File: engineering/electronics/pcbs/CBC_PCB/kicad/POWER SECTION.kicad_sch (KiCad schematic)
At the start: 72 parts, among them J4 AMT0650009DB0000G, J5 AMT0650009DB0000G, J6 AMT0650009DB0000G, J7 AMT0650009DB0000G, Q4 SP015N03BGHTO, U10 CPC1106NTR, U11 CPC1106NTR, U12 74LVC1G17W5-7, U13 74LVC2G02HK3-7, U14 MAX810R, U15 XL7056E1, U16 1kΩ, U17 1kΩ, U18 1kΩ, U19 1kΩ, U20 1kΩ, U21 1kΩ, U22 CPC1019NTR, U31 1kΩ, U32 1kΩ

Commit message: fix: include updated CBC power section
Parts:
- removed C29, C34: 100uF, EasyEDA_Lib:CAP-TH_BD10.0-P5.00-D1.0-FD, symbol EasyEDA_Lib:LKME1252A101MF
- removed C30, C32, C33: 100nF, EasyEDA_Lib:C0603, symbol EasyEDA_Lib:CL10B104KC8NNNC
- removed D5: (no value), EasyEDA_Lib:TO-277A_L5.9-W4.4-LS6.5-TR, symbol EasyEDA_Lib:FSV10150V
- removed L3: 100uH, EasyEDA_Lib:IND-SMD_L7.1-W6.6, symbol EasyEDA_Lib:SMMS0650-101M
- removed R17: 2.7kΩ, EasyEDA_Lib:R0603, symbol EasyEDA_Lib:RT0603BRD072K7L
- removed R18: 23.7kΩ, EasyEDA_Lib:R0603, symbol EasyEDA_Lib:0603WAF2372T5E
- removed R19: 60mΩ, EasyEDA_Lib:R1206, symbol EasyEDA_Lib:JER1206F1R060
- removed U15: XL7056E1, EasyEDA_Lib:TO-263-7_L9.3-W10.0-P1.27-LB-LS15.0, symbol EasyEDA_Lib:XL7056E1
- added C36, C80, C84: 100nF, EasyEDA_Lib:C0603, symbol EasyEDA_Lib:CL10B104KC8NNNC
- added C78, C79: 2.2uF, EasyEDA_Lib:CAP-TH_BD5.0-P2.00-D0.5-FD-1, symbol EasyEDA_Lib:ERJ1KM2R2D11OT
- added C81, C82, C83: 4.7uF, EasyEDA_Lib:C0805, symbol EasyEDA_Lib:CL21A475KBQNNNE
- added D24: (no value), EasyEDA_Lib:TO-277A_L5.9-W4.4-LS6.5-TR, symbol EasyEDA_Lib:FSV10150V
- added D25: (no value), EasyEDA_Lib:SMB_L4.6-W3.6-LS5.3-BI, symbol EasyEDA_Lib:SMBJ5.0CA_C83323
- added L7: 33uH, EasyEDA_Lib:IND-SMD_L8.5-W8.0_SMS0850, symbol EasyEDA_Lib:ZEMS0850-330M
- added R49: 590K, 0603, symbol Device:R
- added R50, R52: 10kΩ, EasyEDA_Lib:R0603, symbol EasyEDA_Lib:RT0603BRD0710KL
- added R51: 140kΩ, EasyEDA_Lib:R0603, symbol EasyEDA_Lib:PTFR0603B140KP9
- added U33: MP9486GN-Z, CBC_PCB:SOIC-8EP_MP9486_MNP, symbol MP9486GN-Z:MP9486GN-Z
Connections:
- net 12V_GATE_V: now also C36.2, C81.2, C82.2, C83.2, L7.2, R49.2
- net H_PWR-IN: now also R51.2
- net H_PWR-IN-: now also C78.2, C79.2, C81.1, C82.1, C83.1, C84.1, D24.1 (A), D24.2 (A), D25.1 (K), R50.1, R52.1, U33.8 (GND)
- net at R48.1: now also C78.1, C79.1, U33.3 (VIN)
- new net: C84.2, D25.2 (A), R51.1, R52.2, U33.6 (DIM), U33.7 (EN)
- new net: C80.1, D24.3 (K), L7.1, U33.5 (SW)
- new net: C36.1, R49.1, R50.2, U33.1 (FB)
- new net: C80.2, U33.4 (BST)
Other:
- moved on the sheet: D10, D11, D12, D13, D22, D23, D6, D7, D8, D9, F1, J6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

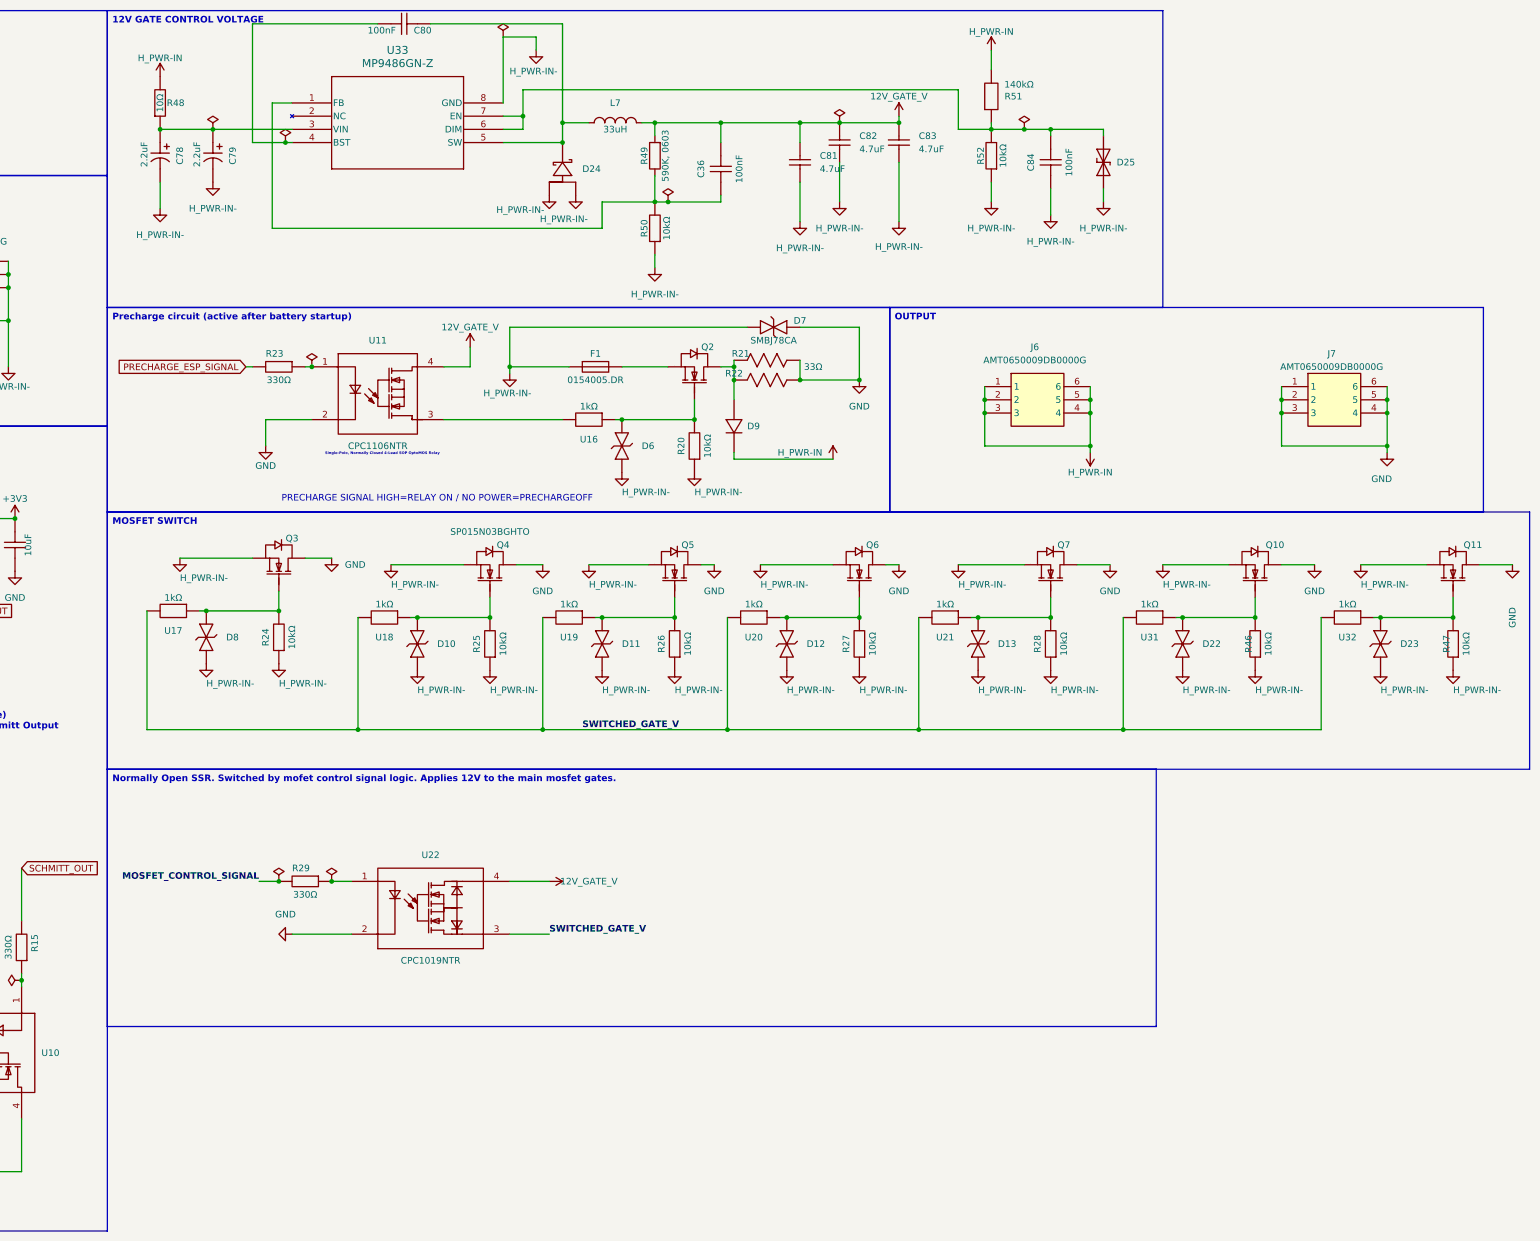
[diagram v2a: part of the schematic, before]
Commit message: electronics: update CBC redundant power regulators
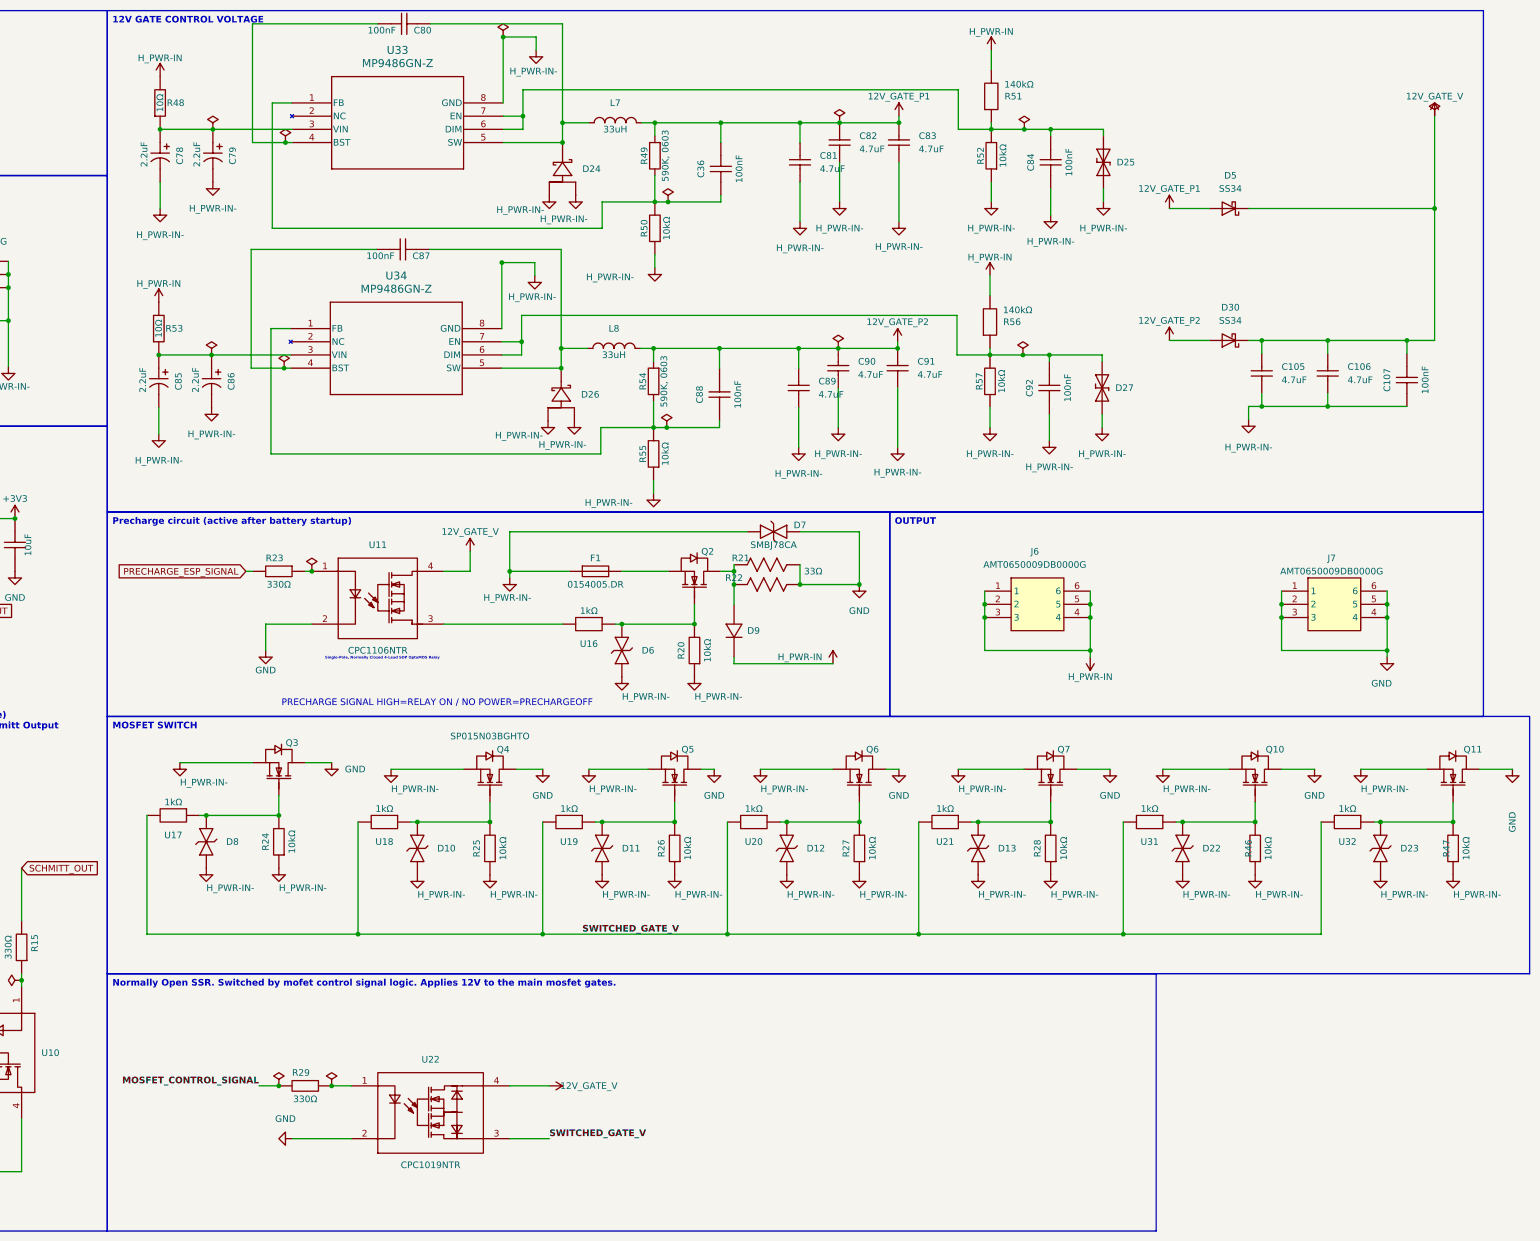
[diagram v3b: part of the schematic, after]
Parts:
- added C105, C106, C89, C90, C91: 4.7uF, EasyEDA_Lib:C0805, symbol EasyEDA_Lib:CL21A475KBQNNNE
- added C107, C87, C88, C92: 100nF, EasyEDA_Lib:C0603, symbol EasyEDA_Lib:CL10B104KC8NNNC
- added C85, C86: 2.2uF, EasyEDA_Lib:CAP-TH_BD5.0-P2.00-D0.5-FD-1, symbol EasyEDA_Lib:ERJ1KM2R2D11OT
- added D26: (no value), EasyEDA_Lib:TO-277A_L5.9-W4.4-LS6.5-TR, symbol EasyEDA_Lib:FSV10150V
- added D27: (no value), EasyEDA_Lib:SMB_L4.6-W3.6-LS5.3-BI, symbol EasyEDA_Lib:SMBJ5.0CA_C83323
- added D30, D5: SS34, Diode_SMD:D_SMA, symbol Diode:SS34
- added L8: 33uH, EasyEDA_Lib:IND-SMD_L8.5-W8.0_SMS0850, symbol EasyEDA_Lib:ZEMS0850-330M
- added R53: 10Ω, EasyEDA_Lib:R2512, symbol EasyEDA_Lib:25121WF100JT4E
- added R54: 590K, 0603, symbol Device:R
- added R55, R57: 10kΩ, EasyEDA_Lib:R0603, symbol EasyEDA_Lib:RT0603BRD0710KL
- added R56: 140kΩ, EasyEDA_Lib:R0603, symbol EasyEDA_Lib:PTFR0603B140KP9
- added U34: MP9486GN-Z, CBC_PCB:SOIC-8EP_MP9486_MNP, symbol MP9486GN-Z:MP9486GN-Z
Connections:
- net 12V_GATE_V: now also C105.2, C106.2, C107.2, D30.1 (K), D5.1 (K); no longer C36.2, C81.2, C82.2, C83.2, L7.2, R49.2
- net H_PWR-IN: now also R53.2, R56.2
- net H_PWR-IN-: now also C105.1, C106.1, C107.1, C85.2, C86.2, C89.1, C90.1, C91.1, C92.1, D26.1 (A), D26.2 (A), D27.1 (K), R55.1, R57.1, U34.8 (GND)
- new net: C88.1, R54.1, R55.2, U34.1 (FB)
- new net: C85.1, C86.1, R53.1, U34.3 (VIN)
- new net: C87.2, U34.4 (BST)
- new net: C87.1, D26.3 (K), L8.1, U34.5 (SW)
- new net: C92.2, D27.2 (A), R56.1, R57.2, U34.6 (DIM), U34.7 (EN)
- new net 12V_GATE_P1: C36.2, C81.2, C82.2, C83.2, D5.2 (A), L7.2, R49.2
- new net 12V_GATE_P2: C88.2, C89.2, C90.2, C91.2, D30.2 (A), L8.2, R54.2
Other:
- moved on the sheet: D10, D11, D12, D13, D22, D23, D6, D7, D8, D9, F1, J6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
